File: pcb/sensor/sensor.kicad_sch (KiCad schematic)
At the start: 39 parts, among them J3 sig_in, J4 sig_out, J5 Conn_01x02_Pin, J6 Conn_01x02_Pin, J7 Conn_02x02_Counter_Clockwise, U1 TJA1051T-3, U2 HX711, U3 LM2595S-3.3, U4 LM2595S-5, U5 LMR16030SDDAR

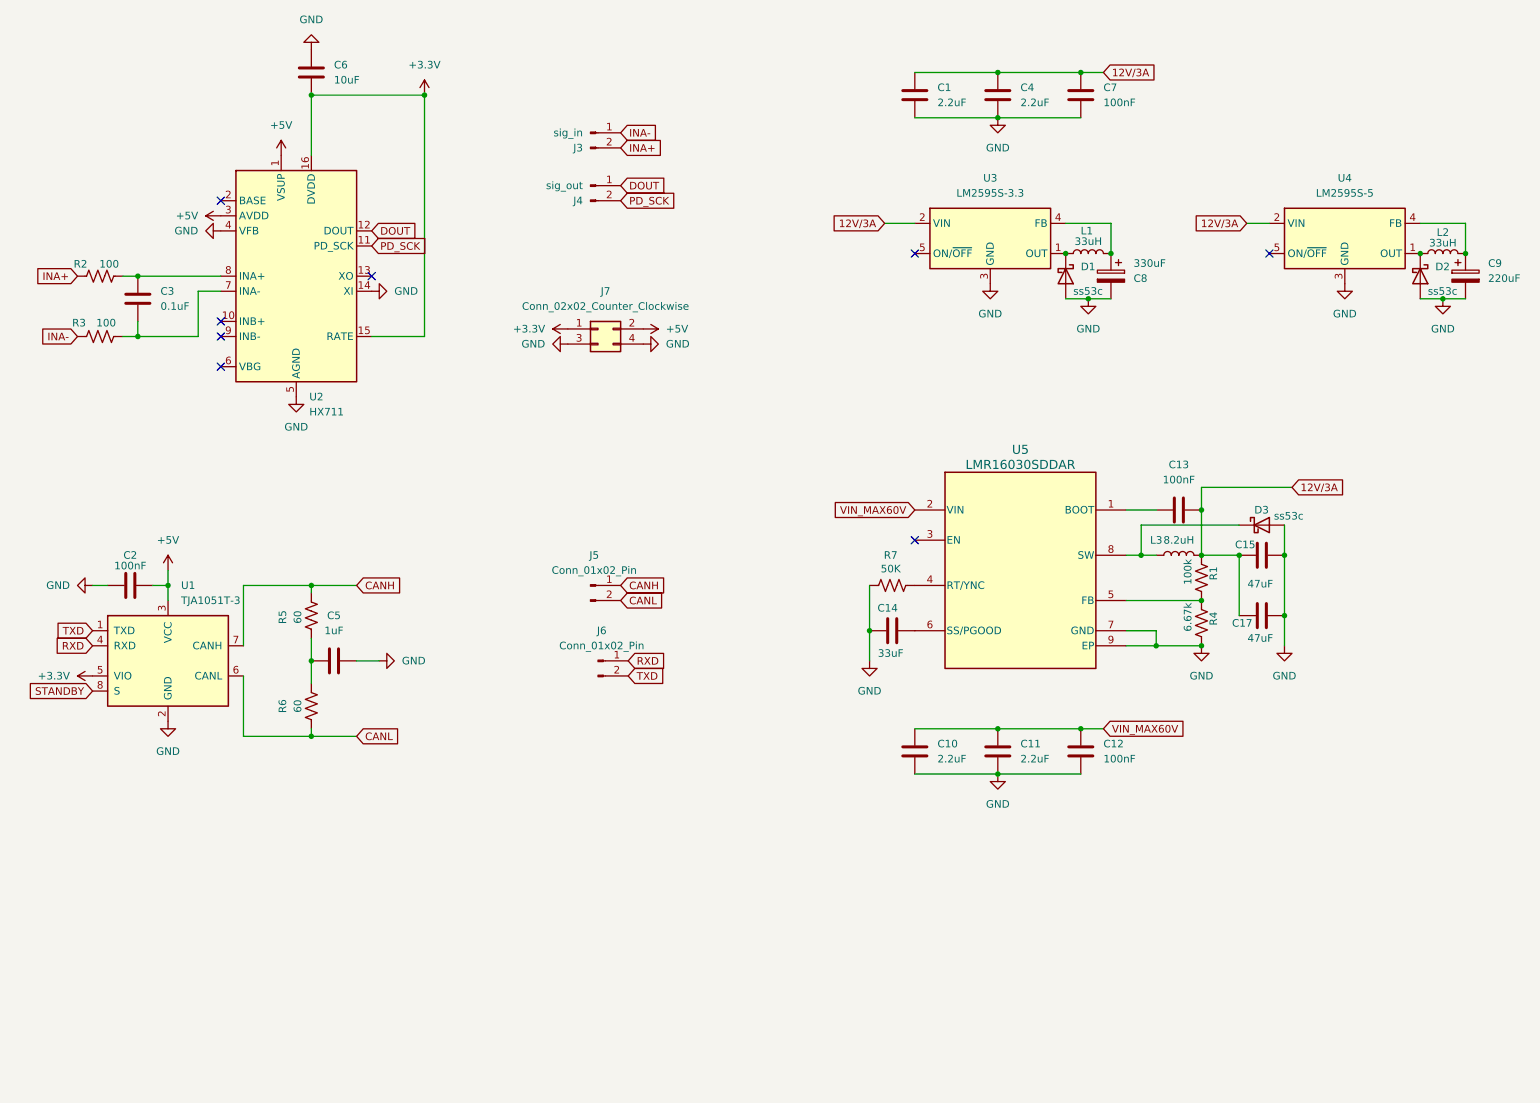
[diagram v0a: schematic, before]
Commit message: feat: update dc-dc
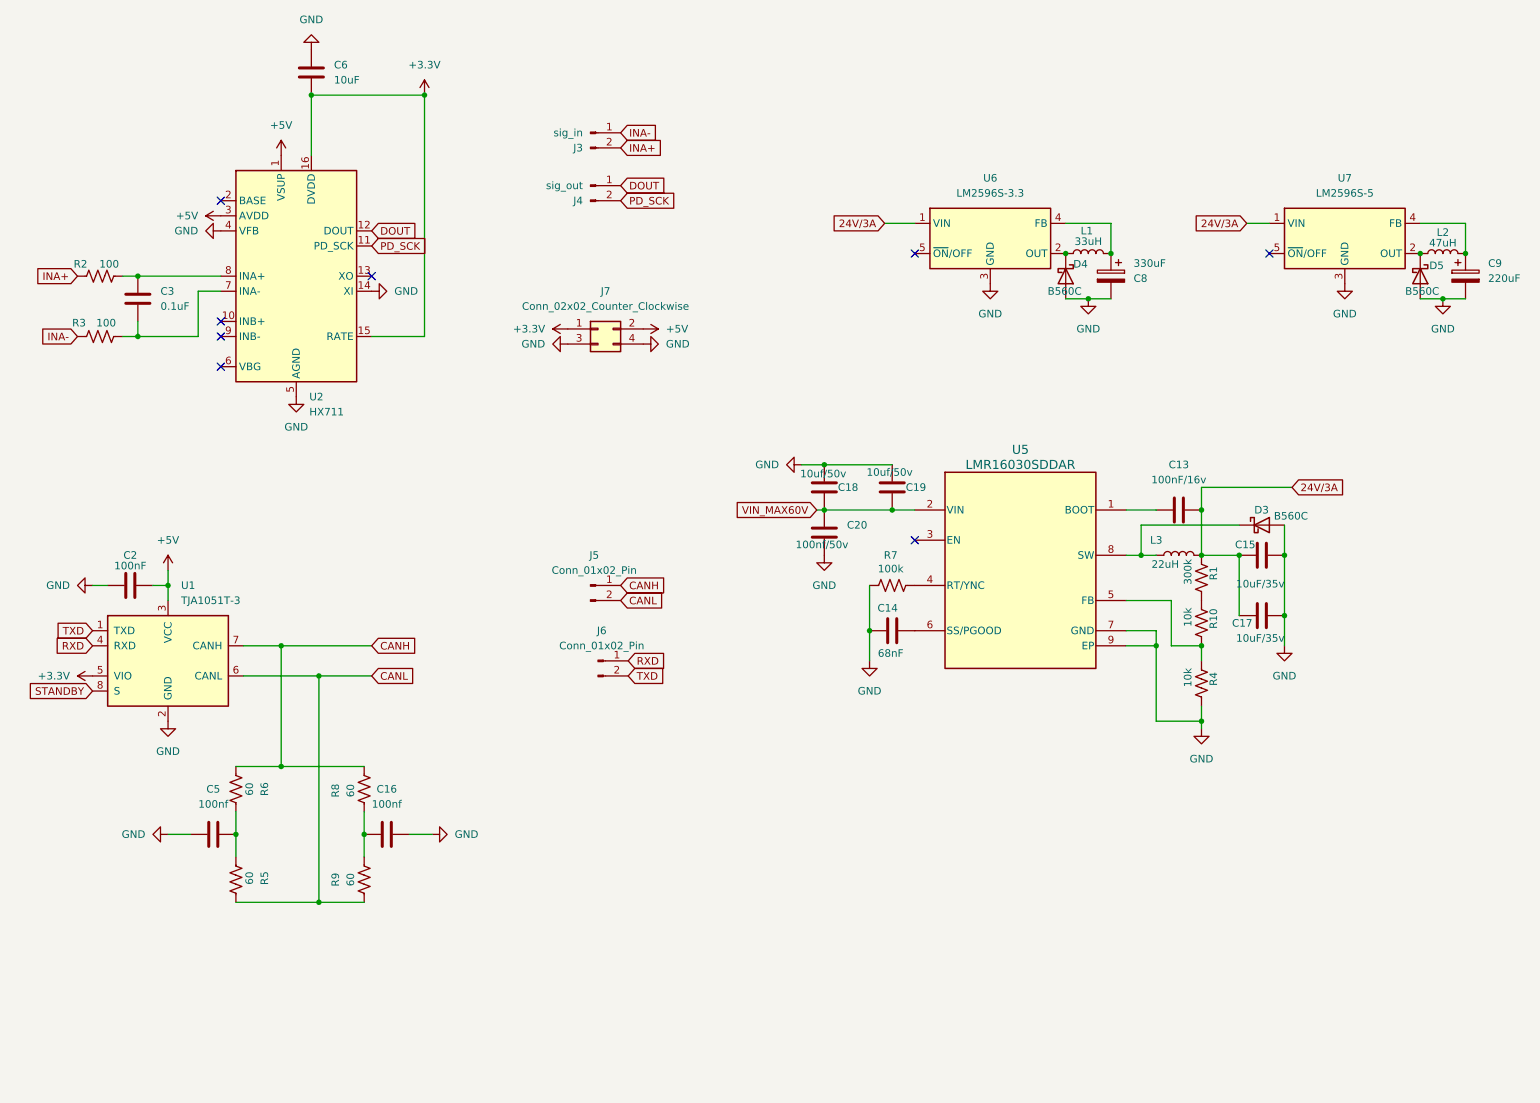
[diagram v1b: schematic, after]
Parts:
- removed C1, C10, C11, C4: 2.2uF, symbol Device:C
- removed C12, C7: 100nF, Capacitor_SMD:C_0603_1608Metric, symbol Device:C
- removed D1, D2: ss53c, symbol Device:D_Schottky
- removed U3: LM2595S-3.3, Package_TO_SOT_SMD:TO-263-5_TabPin3, symbol Regulator_Switching:LM2595S-3.3
- removed U4: LM2595S-5, Package_TO_SOT_SMD:TO-263-5_TabPin3, symbol Regulator_Switching:LM2595S-5
- added C16: 100nf, Capacitor_SMD:C_0603_1608Metric, symbol Device:C
- added C18, C19: 10uf/50v, Capacitor_SMD:C_1210_3225Metric, symbol Device:C
- added C20: 100nf/50v, Capacitor_SMD:C_1210_3225Metric, symbol Device:C
- added D4, D5: B560C, Diode_SMD:D_SMC, symbol Device:D_Schottky
- added R10: 10k, Resistor_SMD:R_0603_1608Metric, symbol Device:R_US
- added R8, R9: 60, Resistor_SMD:R_0603_1608Metric, symbol Device:R_US
- added U6: LM2596S-3.3, Package_TO_SOT_SMD:TO-263-5_TabPin3, symbol Regulator_Switching:LM2596S-3.3
- added U7: LM2596S-5, Package_TO_SOT_SMD:TO-263-5_TabPin3, symbol Regulator_Switching:LM2596S-5
- C13: value 100nF -> 100nF/16v
- C14: value 33uF -> 68nF; footprint (none) -> Capacitor_SMD:C_0603_1608Metric
- C15: value 47uF -> 10uF/35v; footprint (none) -> Capacitor_SMD:C_1206_3216Metric
- C17: value 47uF -> 10uF/35v; footprint (none) -> Capacitor_SMD:C_1210_3225Metric
- C5: value 1uF -> 100nf
- D3: value ss53c -> B560C; footprint (none) -> Diode_SMD:D_SMC
- L2: value 33uH -> 47uH
- L3: value 8.2uH -> 22uH; footprint (none) -> Inductor_SMD:L_Changjiang_FXL0650
- R1: value 100k -> 300k
- R4: value 6.67k -> 10k
- R7: value 50K -> 100k
- U5: footprint DDA0008E_N -> Package_SO:TI_SO-PowerPAD-8_ThermalVias
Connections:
- net CANH: now also R6.1, R8.2; no longer R5.2
- net CANL: now also R5.2, R9.1; no longer R6.1
- net GND: now also C16.1, C18.2, C19.1, C20.2, D4.2 (A), D5.2 (A), U6.3 (GND), U7.3 (GND)
- net VIN_MAX60V: now also C18.1, C19.2, C20.1
- net at R4.1, U5.5 (FB): now also R10.2; no longer R1.2
- net at L2.1: now also D5.1 (K), U7.2 (OUT)
- net at C9.1, L2.2: now also U7.4 (FB)
- net at L1.1: now also D4.1 (K), U6.2 (OUT)
- net at C8.1, L1.2: now also U6.4 (FB)
- net 12V/3A renamed 24V/3A
- net 24V/3A: now also U6.1 (VIN), U7.1 (VIN)
- new net: C16.2, R8.1, R9.2
- new net: R1.2, R10.1
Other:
- moved on the sheet: C5, R4, R5, R6

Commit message: feat: add dc-dc compute script
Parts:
- removed C8: 330uF, symbol Device:C_Polarized
- removed C9: 220uF, symbol Device:C_Polarized
- removed D4, D5: B560C, Diode_SMD:D_SMC, symbol Device:D_Schottky
- removed L1: 33uH, symbol Device:L
- removed L2: 47uH, symbol Device:L
- removed U6: LM2596S-3.3, Package_TO_SOT_SMD:TO-263-5_TabPin3, symbol Regulator_Switching:LM2596S-3.3
- removed U7: LM2596S-5, Package_TO_SOT_SMD:TO-263-5_TabPin3, symbol Regulator_Switching:LM2596S-5
- added C21, C23, C28, C30: 4.7uf/50v, Capacitor_SMD:C_1210_3225Metric, symbol Device:C
- added C22, C29: 100nf/50v, Capacitor_SMD:C_1210_3225Metric, symbol Device:C
- added C24, C31: 47nF, Capacitor_SMD:C_0603_1608Metric, symbol Device:C
- added C25, C32: 100nF/16v, Capacitor_SMD:C_0603_1608Metric, symbol Device:C
- added C26: 22uF/10v, Capacitor_SMD:C_1206_3216Metric, symbol Device:C
- added C27: 22uF/10v, Capacitor_SMD:C_1210_3225Metric, symbol Device:C
- added C33: 22uF/16v, Capacitor_SMD:C_1206_3216Metric, symbol Device:C
- added C34: 22uF/16v, Capacitor_SMD:C_1210_3225Metric, symbol Device:C
- added D6, D7: B560C, Diode_SMD:D_SMC, symbol Device:D_Schottky
- added L4: 22uH, Inductor_SMD:L_Changjiang_FXL0650, symbol Device:L
- added L5: 47uH, Inductor_SMD:L_Changjiang_FXL0650, symbol Device:L
- added R11: 56k, Resistor_SMD:R_0603_1608Metric, symbol Device:R_US
- added R12: 22k, Resistor_SMD:R_0603_1608Metric, symbol Device:R_US
- added R13: 600, Resistor_SMD:R_0603_1608Metric, symbol Device:R_US
- added R14, R18: 10k, Resistor_SMD:R_0603_1608Metric, symbol Device:R_US
- added R15: 100k, Resistor_SMD:R_0603_1608Metric, symbol Device:R_US
- added R16: 39k, Resistor_SMD:R_0603_1608Metric, symbol Device:R_US
- added R17: 1.2k, Resistor_SMD:R_0603_1608Metric, symbol Device:R_US
- added R19, R20: 820, Resistor_SMD:R_0603_1608Metric, symbol Device:R_US
- added U8, U9: LMR16030SDDAR, Package_SO:TI_SO-PowerPAD-8_ThermalVias, symbol 2025-01-08_11-11-09:LMR16030SDDAR
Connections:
- net 24V/3A: now also C21.1, C22.1, C23.2, U8.2 (VIN)
- net GND: now also C21.2, C22.2, C23.1, C24.2, C26.2, C27.1, C28.2, C29.2, C30.1, C31.2, C33.2, C34.1, D6.2 (A), D7.2 (A), R14.2, R18.2, R19.2, R20.2, U8.7 (GND), U8.9 (EP), U9.7 (GND), U9.9 (EP)
- net VIN_MAX60V: now also C28.1, C29.1, C30.2, U9.2 (VIN)
- new net: C25.2, U8.1 (BOOT)
- new net: D6.1 (K), L4.1, U8.8 (SW)
- new net: R16.2, R17.1
- new net: R17.2, R18.1, U9.5 (FB)
- new net: R15.2, R20.1
- new net: R13.2, R14.1, U8.5 (FB)
- new net: D7.1 (K), L5.1, U9.8 (SW)
- new net: C31.1, U9.6 (SS/PGOOD)
- new net: C32.2, U9.1 (BOOT)
- new net: R15.1, U9.4 (RT/YNC)
- new net: R12.2, R13.1
- new net: R11.1, U8.4 (RT/YNC)
- new net: R11.2, R19.1
- new net: C24.1, U8.6 (SS/PGOOD)
- new net 3.3V/3A: C25.1, C26.1, C27.2, L4.2, R12.1
- new net 5V/3A: C32.1, C33.1, C34.2, L5.2, R16.1
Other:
- moved on the sheet: C13, C14, C15, C16, C17, C18, C19, C2, C20, C3, C5, C6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

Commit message: feat: update sch adn scripts
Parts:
- removed C23: 4.7uf/50v, Capacitor_SMD:C_1210_3225Metric, symbol Device:C
- removed C29: 100nf/50v, Capacitor_SMD:C_1210_3225Metric, symbol Device:C
- C15: footprint Capacitor_SMD:C_1206_3216Metric -> Capacitor_SMD:C_1210_3225Metric
- C20, C22: footprint Capacitor_SMD:C_1210_3225Metric -> Capacitor_SMD:C_0603_1608Metric
- C21, C28, C30: footprint Capacitor_SMD:C_1210_3225Metric -> Capacitor_SMD:C_1206_3216Metric
- C26: value 22uF/10v -> 10uF/10v; footprint Capacitor_SMD:C_1206_3216Metric -> Capacitor_SMD:C_0603_1608Metric
- C27: value 22uF/10v -> 10uF/10v; footprint Capacitor_SMD:C_1210_3225Metric -> Capacitor_SMD:C_0603_1608Metric
- C33: value 22uF/16v -> 10uF/16v; footprint Capacitor_SMD:C_1206_3216Metric -> Capacitor_SMD:C_1210_3225Metric
- C34: value 22uF/16v -> 10uF/16v
- L3, L4, L5: footprint Inductor_SMD:L_Changjiang_FXL0650 -> Inductor_SMD:L_TDK_SLF12565
- R11: value 56k -> 62k
- R12: value 22k -> 33k
- R13: value 600 -> 1k
- R15: value 100k -> 62k
- R16: value 39k -> 56k
- R17: value 1.2k -> 680
- R19, R20: value 820 -> 1.3k
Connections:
- net 24V/3A: now also C21.2, C28.1, C30.2, U9.2 (VIN); no longer C21.1
- net GND: now also C21.1; no longer C21.2
- net VIN_MAX60V: no longer C28.1, C30.2, U9.2 (VIN)
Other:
- moved on the sheet: C21, C22, C28, C30
